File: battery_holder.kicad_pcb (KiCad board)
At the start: 2 copper layers, 30 x 20 mm, 14 parts, among them J1 aux pwr, J2 usb, J3 TP4056, J4 aux bat, J5 Bat+, J6 Bat-

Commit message: Updates according to newest template
- added logo
- changed to new format of .gitignore
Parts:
- added G***: LOGO, LOGO, B.Cu at (89.7, 44.0)
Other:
- board text added: "v1.0 (2022)"
- board text removed: "chof (c) 2022"

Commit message: Added +/- signs on input pins
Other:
- board text added: "+"
- board text added: "-"
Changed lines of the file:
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@@
     (effects (font (size 1 1) (thickness 0.15)) (justify left mirror))
+  )
+  (gr_text "+" (at 77.216 38.1) (layer "F.SilkS")
+    (effects (font (size 1.2 1.2) (thickness 0.15)))
+  )
+  (gr_text "-" (at 77.18 46.482) (layer "F.SilkS")
+    (effects (font (size 1.2 1.2) (thickness 0.15)))
   )
   (dimension (type aligned) (layer "Cmts.User")
     (pts (xy 71.12 35.56) (xy 71.12 50.292))
     (height 15.24)
-    (gr_text "14,7320 mm" (at 54.73 42.926 90) (layer "Cmts.User")
+    (gr_text "14.7320 mm" (at 54.73 42.926 90) (layer "Cmts.User")
       (effects (font (size 1 1) (thickness 0.15)))
     )
@@
     (pts (xy 98.58 52.324) (xy 68.58 52.324))
     (height -5.08)
-    (gr_text "30,0000 mm" (at 83.58 56.254) (layer "Cmts.User")
+    (gr_text "30.0000 mm" (at 83.58 56.254) (layer "Cmts.User")
       (effects (font (size 1 1) (thickness 0.15)))
     )
@@
     (pts (xy 68.695 38.966) (xy 68.695 46.826))
     (height 5.703)
-    (gr_text "7,8600 mm" (at 61.842 42.896 90) (layer "Cmts.User")
+    (gr_text "7.8600 mm" (at 61.842 42.896 90) (layer "Cmts.User")
       (effects (font (size 1 1) (thickness 0.15)))
     )
@@
     (pts (xy 97.028 38.349) (xy 97.028 46.477))
     (height -8.636)
-    (gr_text "8,1280 mm" (at 104.514 42.413 90) (layer "Cmts.User")
+    (gr_text "8.1280 mm" (at 104.514 42.413 90) (layer "Cmts.User")
       (effects (font (size 1 1) (thickness 0.15)))
     )
@@
     (pts (xy 98.58 33.02) (xy 98.58 53.02))
     (height -13.716)
-    (gr_text "20,0000 mm" (at 111.146 43.02 90) (layer "Cmts.User")
+    (gr_text "20.0000 mm" (at 111.146 43.02 90) (layer "Cmts.User")
       (effects (font (size 1 1) (thickness 0.15)))
     )
@@
     (pts (xy 96.012 35.56) (xy 71.12 35.56))
     (height 22.56458)
-    (gr_text "24,8920 mm" (at 83.566 11.84542) (layer "Cmts.User")
+    (gr_text "24.8920 mm" (at 83.566 11.84542) (layer "Cmts.User")
       (effects (font (size 1 1) (thickness 0.15)))
     )

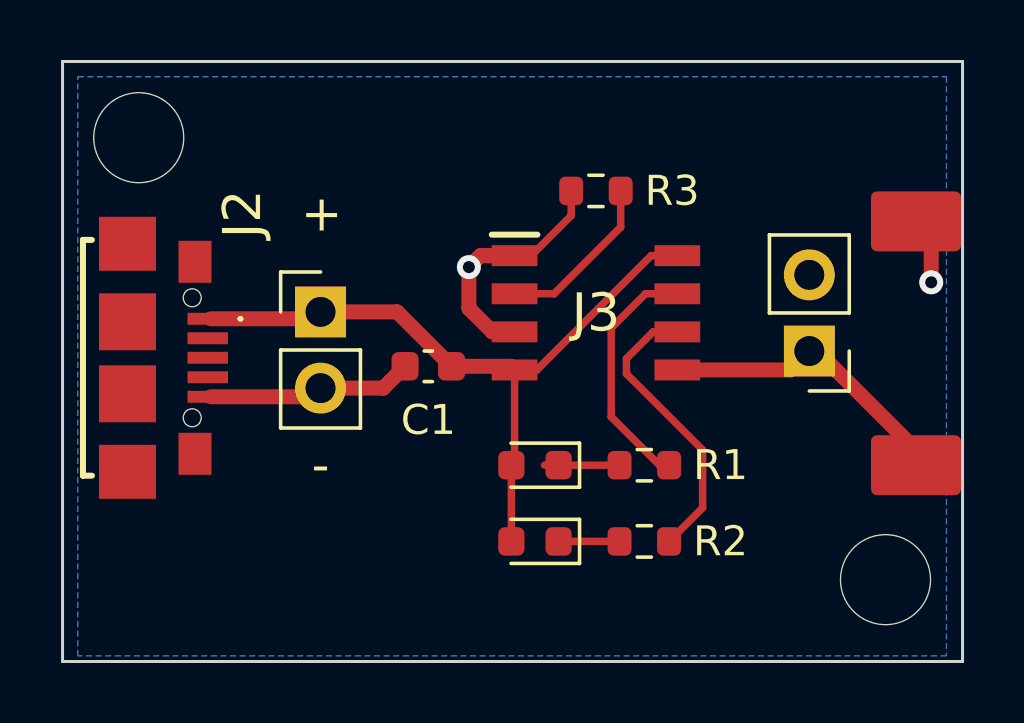
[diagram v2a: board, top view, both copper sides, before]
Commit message: Updated template for KiCAD 7
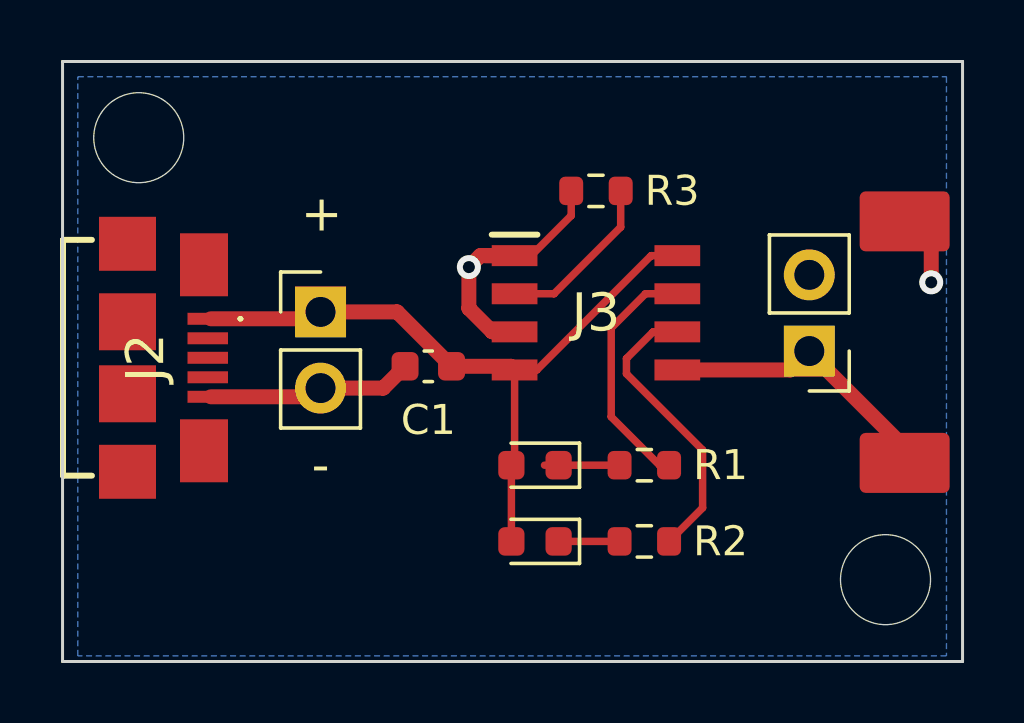
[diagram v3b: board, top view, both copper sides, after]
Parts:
- J2: footprint footprints:MU-101-ACY -> Chof747 Footprints:101181920002LF
- moved J5 0.39 mm to (96.7, 46.4)
- moved J6 0.38 mm to (96.7, 38.3)
